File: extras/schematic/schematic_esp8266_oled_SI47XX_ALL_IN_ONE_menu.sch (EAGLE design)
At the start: 20 parts, among them U1 SI4735-D60-GU, U2 ESP8266

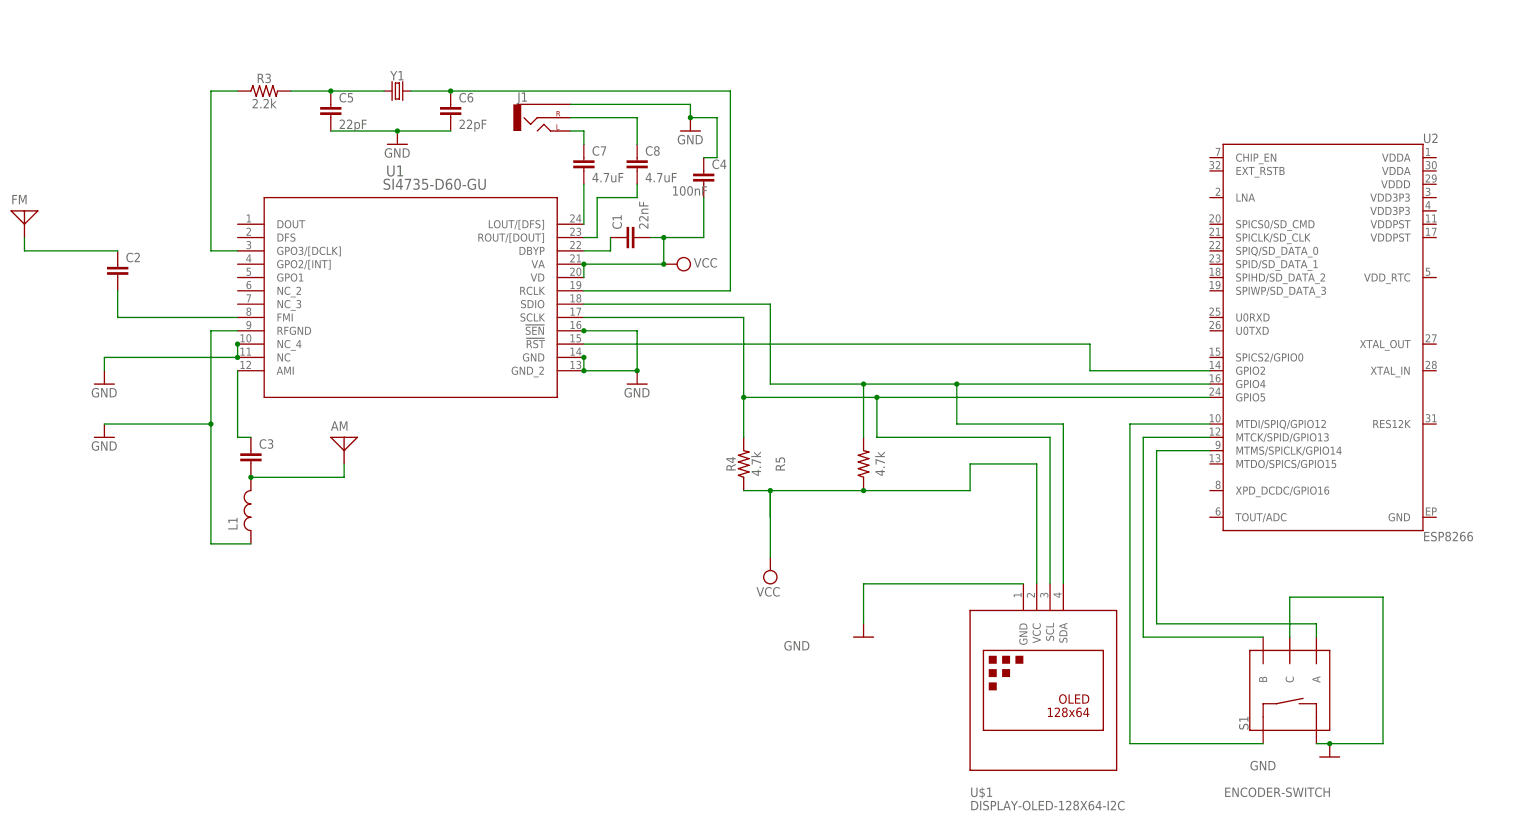
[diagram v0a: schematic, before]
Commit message: SI473X Arduino Library
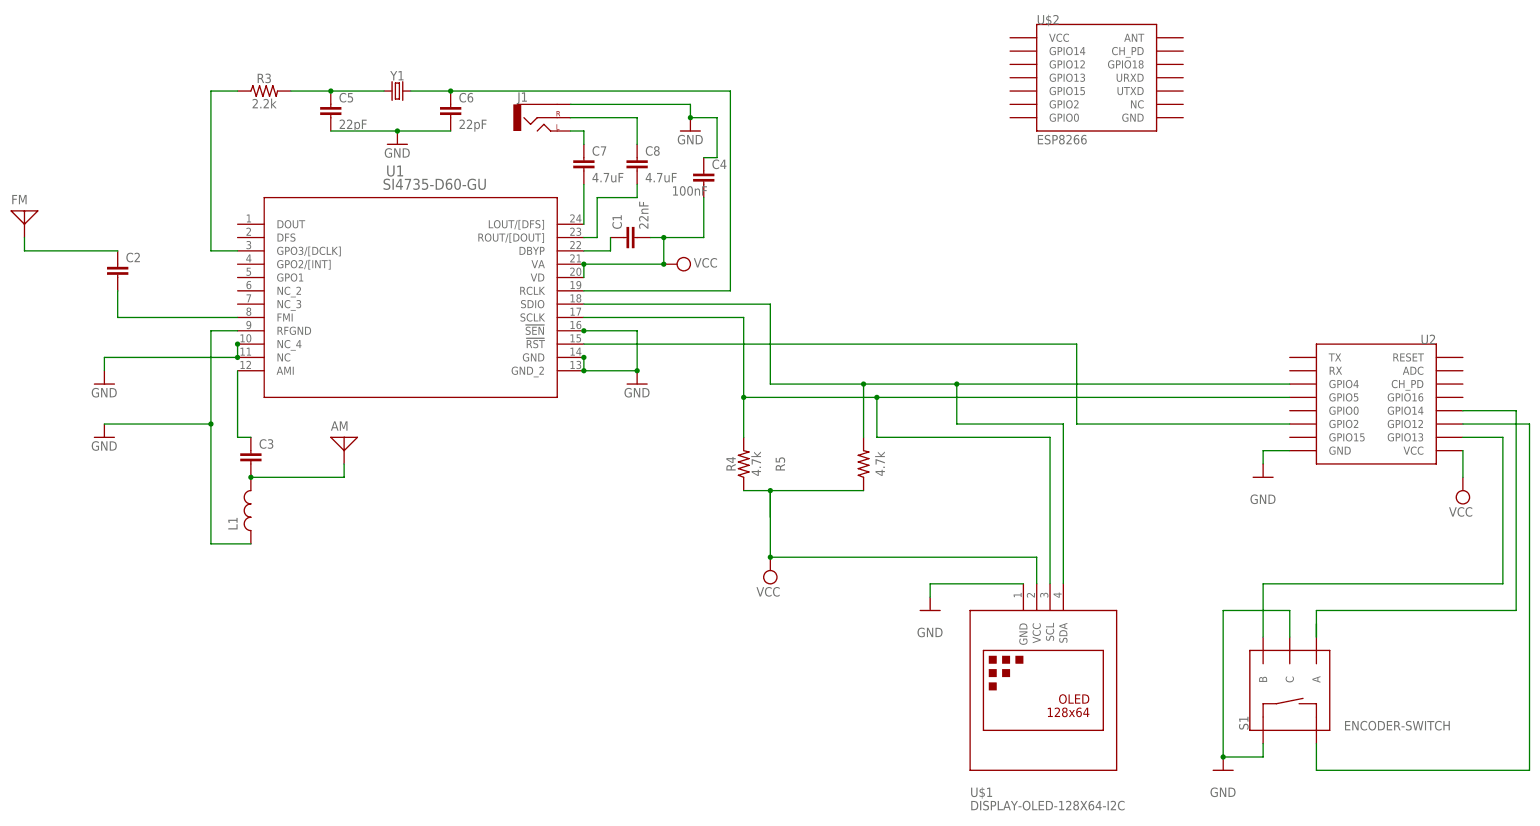
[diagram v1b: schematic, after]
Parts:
- added U$2: ESP8266, esp8266modules:ESP8266
- U2: value ESP8266 -> (none); device SparkFun-RF:ESP8266 -> esp8266modules:ESP12SMD
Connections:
- removed net N$16: S1.B, U2.MTCK/SPID/GPIO13
- new net N$19: S1.SW-, U2.GPIO12
- net GND: now also S1.SW+, U2.GND; no longer S1.SW-
- net N$15: now also S1.B, U2.GPIO13; no longer S1.SW+, U2.MTDI/SPIQ/GPIO12
- net N$17: now also U2.GPIO14; no longer U2.MTMS/SPICLK/GPIO14
- net VCC: now also U2.VCC

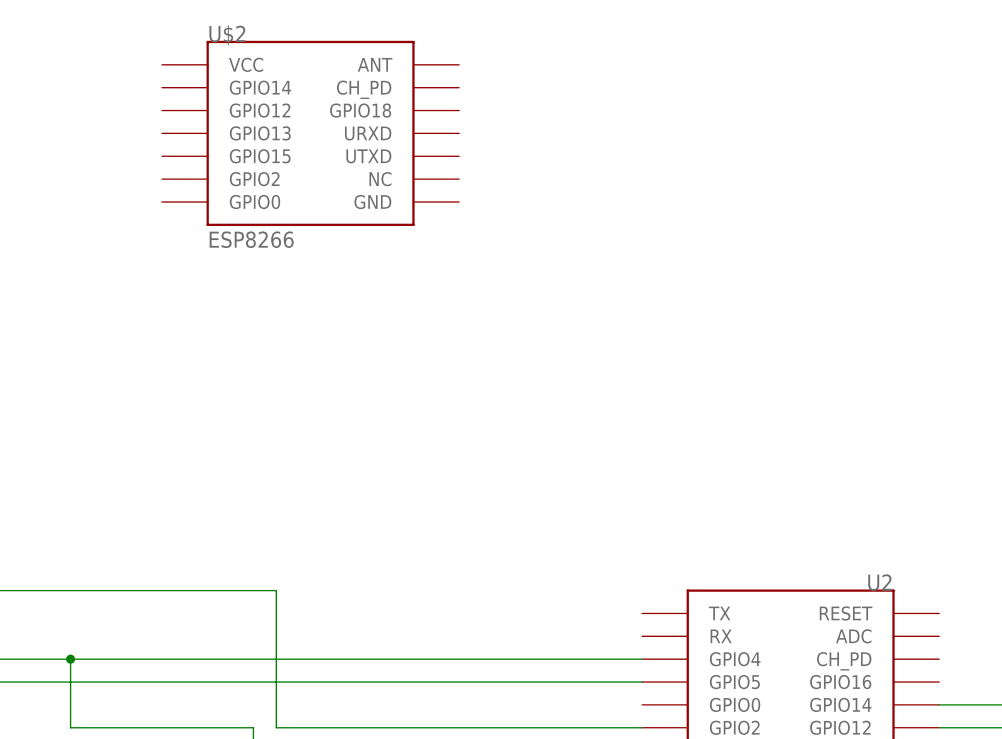
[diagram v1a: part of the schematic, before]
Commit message: SI473X Arduino Library
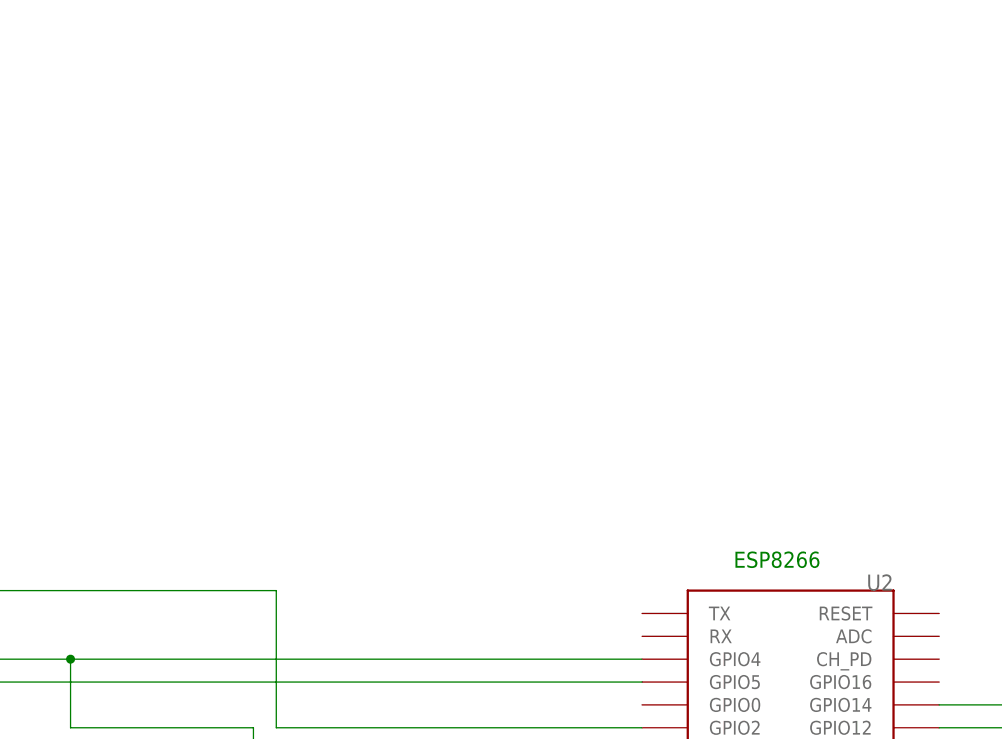
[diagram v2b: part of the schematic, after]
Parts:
- removed U$2: ESP8266, esp8266modules:ESP8266
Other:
- note added: "ESP8266"
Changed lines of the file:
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@@
 <part name="GND2" library="supply1" library_urn="urn:adsk.eagle:library:371" deviceset="GND" device=""/>
 <part name="S1" library="SparkFun-Switches" library_urn="urn:adsk.eagle:library:535" deviceset="ENCODER-SWITCH" device="" package3d_urn="urn:adsk.eagle:package:40158/1"/>
-<part name="U$2" library="esp8266modules" deviceset="ESP8266" device=""/>
 <part name="U2" library="esp8266modules" deviceset="ESP12" device="SMD"/>
 <part name="GND6" library="supply1" library_urn="urn:adsk.eagle:library:371" deviceset="GND" device=""/>
@@
 <rectangle x1="-182.88" y1="226.06" x2="-167.64" y2="241.3" layer="205"/>
 <text x="-180.34" y="243.84" size="1.778" layer="205">Optional</text>
+<text x="30.48" y="187.96" size="1.778" layer="91">ESP8266</text>
 </plain>
 <instances>
@@
 <attribute name="VALUE" x="51.054" y="111.76" size="1.778" layer="96" font="vector" rot="R180" align="top-left"/>
 </instance>
-<instance part="U$2" gate="G$1" x="-15.24" y="236.22" smashed="yes">
-<attribute name="VALUE" x="-27.94" y="223.52" size="1.778" layer="96"/>
-<attribute name="NAME" x="-27.94" y="246.38" size="1.778" layer="95"/>
-</instance>
 <instance part="U2" gate="G$1" x="35.56" y="175.26" smashed="yes" rot="MR0">
